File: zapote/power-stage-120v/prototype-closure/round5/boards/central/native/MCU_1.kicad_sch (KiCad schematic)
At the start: 3 parts, among them J11 B6B-XH-A(LF)(SN)

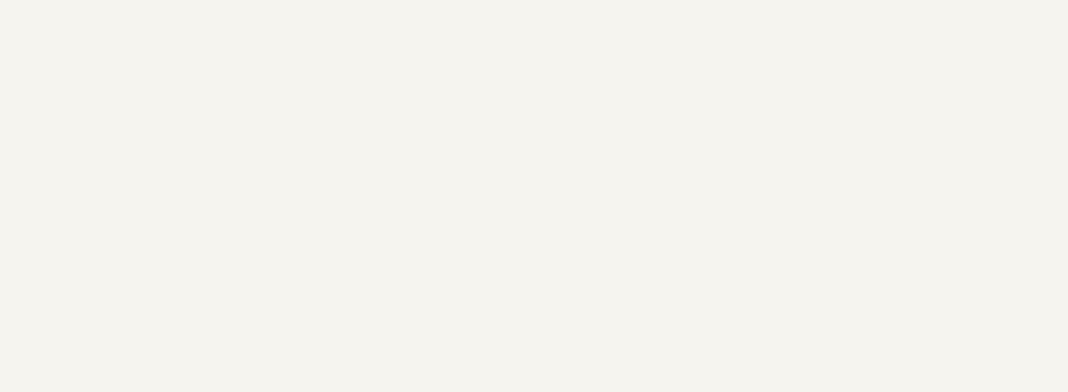
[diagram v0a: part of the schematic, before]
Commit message: WIP snapshot of worktrees/mit-product-guidance (2026-10-08)
Uncommitted Codex prototype-closure work (round5 boards, round6
investigation, firmware power adapter), snapshotted without touching the
worktree. Raw solver output under output/temper-prototype-closure/ is
not included.

Co-Authored-By: Claude Opus 5.5 (1M context) <noreply@anthropic.com>
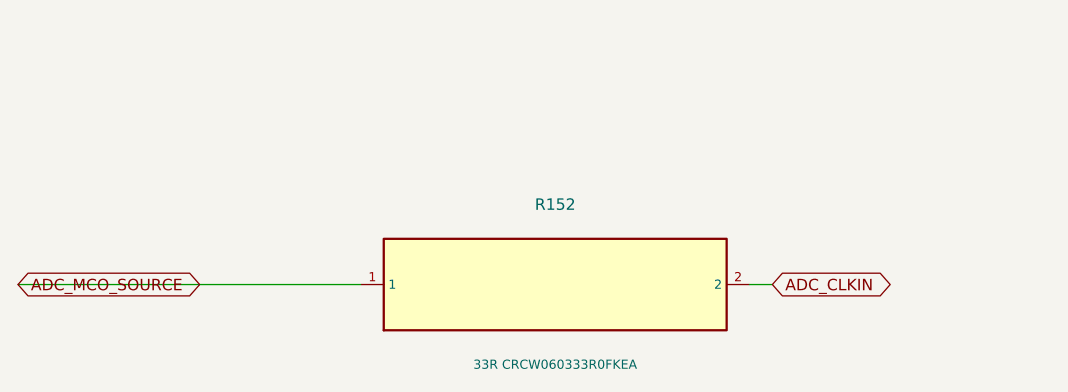
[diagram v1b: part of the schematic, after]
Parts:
- added R152: 33R CRCW060333R0FKEA, Resistor_SMD:R_0603_1608Metric, symbol Supervisor:Part_R152
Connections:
- new net ADC_CLKIN: R152.2
- new net ADC_MCO_SOURCE: R152.1
